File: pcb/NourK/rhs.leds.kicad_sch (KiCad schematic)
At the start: 33 parts

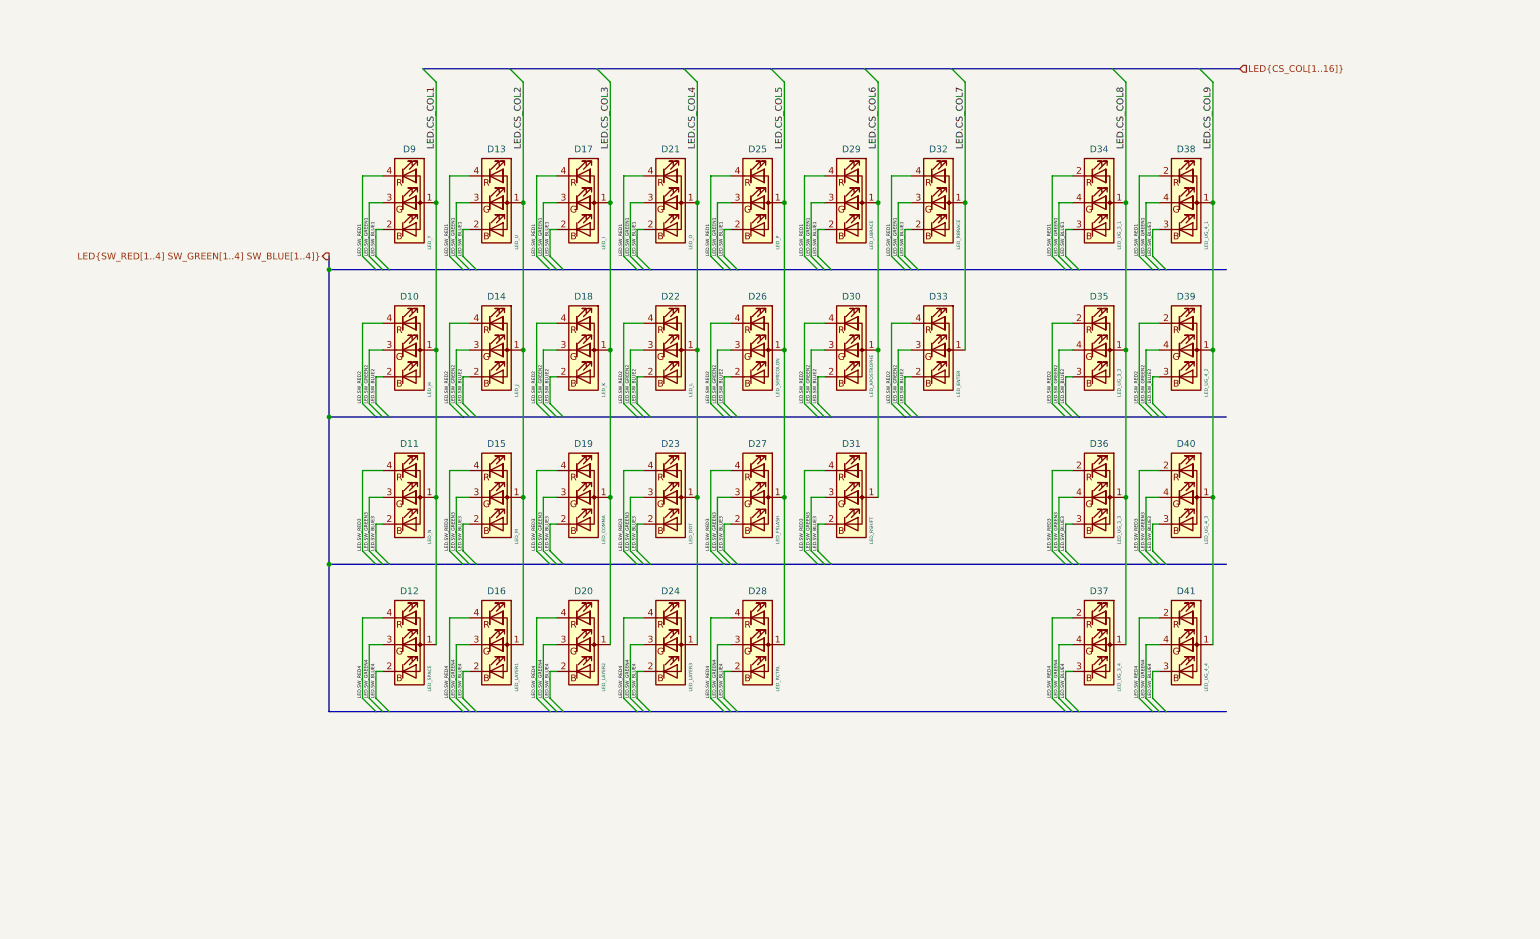
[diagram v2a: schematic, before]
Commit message: Re-traced RHS
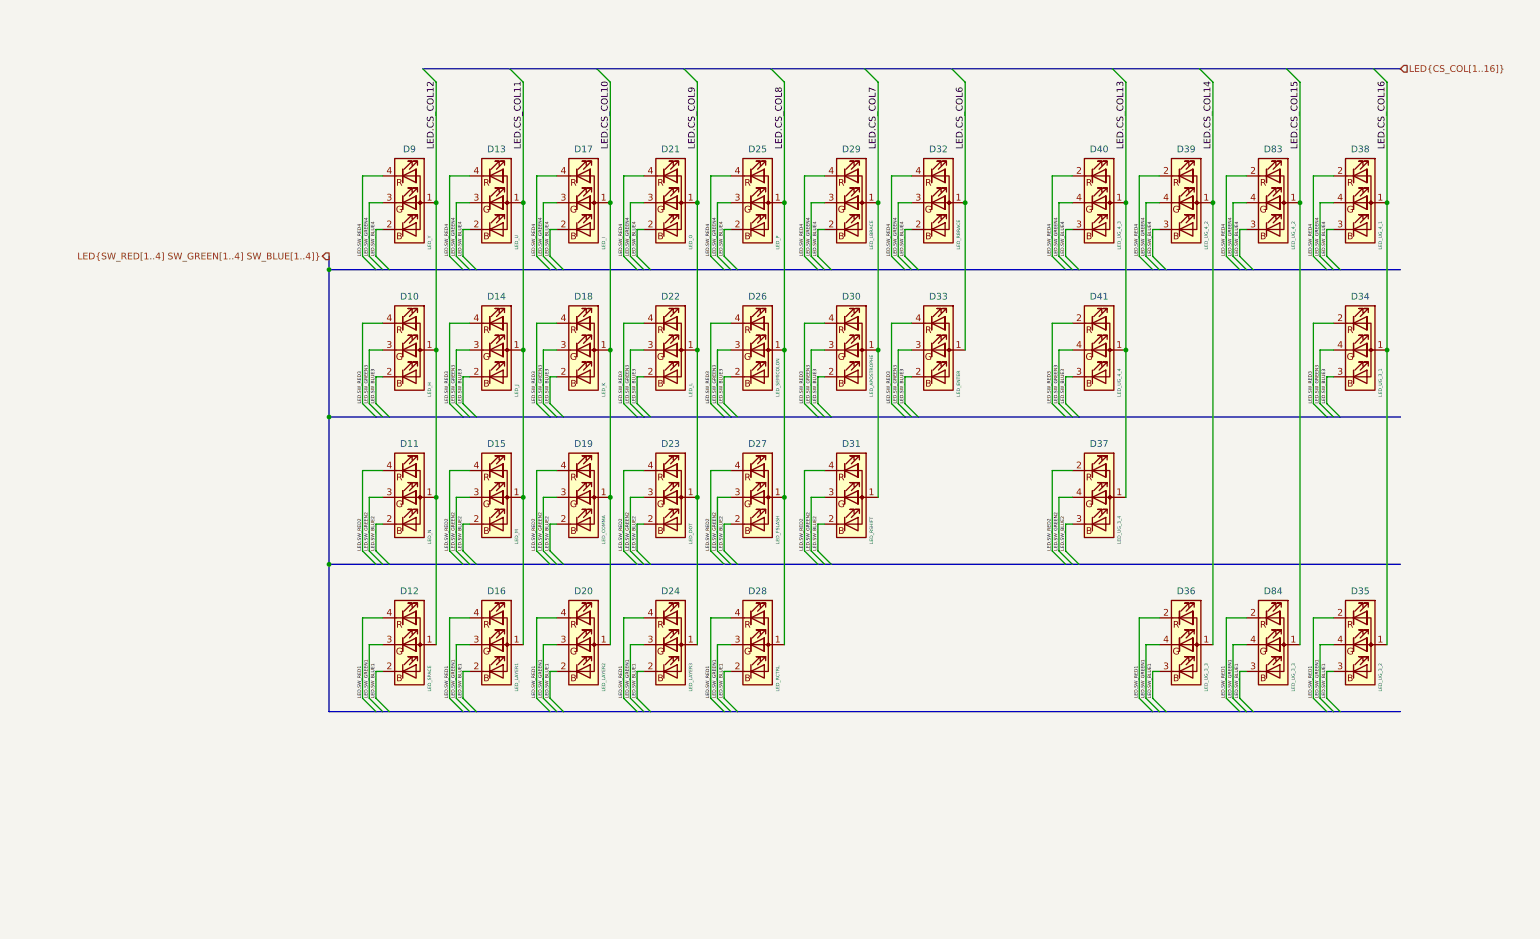
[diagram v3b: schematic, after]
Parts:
- added D83: LED_UG_4_2, Nour_KB:LTRBR37G4R4S012502R18, symbol Device:LED_ARBG
- added D84: LED_UG_3_3, Nour_KB:LTRBR37G4R4S012502R18, symbol Device:LED_ARBG
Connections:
- net LED.CS_COL4 is gone; now on net LED.CS_COL9: D21.1 (A), D22.1 (A), D23.1 (A), D24.1 (A)
- net LED.CS_COL5 is gone; now on net LED.CS_COL8: D25.1 (A), D26.1 (A), D27.1 (A), D28.1 (A)
- net LED.CS_COL6: now also D32.1 (A), D33.1 (A); no longer D29.1 (A), D30.1 (A), D31.1 (A)
- net LED.CS_COL7: now also D29.1 (A), D30.1 (A), D31.1 (A); no longer D32.1 (A), D33.1 (A)
- net LED.CS_COL8: no longer D34.1 (A), D35.1 (A), D36.1 (A), D37.1 (A)
- net LED.CS_COL9: no longer D38.1 (A), D39.1 (A), D40.1 (A), D41.1 (A)
- net LED.SW_BLUE1: now also D12.2 (BK), D16.2 (BK), D20.2 (BK), D24.2 (BK), D28.2 (BK), D35.3 (BK), D36.3 (BK), D84.3 (BK); no longer D13.2 (BK), D17.2 (BK), D21.2 (BK), D25.2 (BK), D29.2 (BK), D32.2 (BK), D34.3 (BK), D38.3 (BK), D9.2 (BK)
- net LED.SW_BLUE2: now also D11.2 (BK), D15.2 (BK), D19.2 (BK), D23.2 (BK), D27.2 (BK), D31.2 (BK), D37.3 (BK); no longer D10.2 (BK), D14.2 (BK), D18.2 (BK), D22.2 (BK), D26.2 (BK), D30.2 (BK), D33.2 (BK), D35.3 (BK), D39.3 (BK)
- net LED.SW_BLUE3: now also D10.2 (BK), D14.2 (BK), D18.2 (BK), D22.2 (BK), D26.2 (BK), D30.2 (BK), D33.2 (BK), D34.3 (BK), D41.3 (BK); no longer D11.2 (BK), D15.2 (BK), D19.2 (BK), D23.2 (BK), D27.2 (BK), D31.2 (BK), D36.3 (BK), D40.3 (BK)
- net LED.SW_BLUE4: now also D13.2 (BK), D17.2 (BK), D21.2 (BK), D25.2 (BK), D29.2 (BK), D32.2 (BK), D38.3 (BK), D39.3 (BK), D40.3 (BK), D9.2 (BK), D83.3 (BK); no longer D12.2 (BK), D16.2 (BK), D20.2 (BK), D24.2 (BK), D28.2 (BK), D37.3 (BK), D41.3 (BK)
- net LED.SW_GREEN1: now also D12.3 (GK), D16.3 (GK), D20.3 (GK), D24.3 (GK), D28.3 (GK), D35.4 (GK), D36.4 (GK), D84.4 (GK); no longer D13.3 (GK), D17.3 (GK), D21.3 (GK), D25.3 (GK), D29.3 (GK), D32.3 (GK), D34.4 (GK), D38.4 (GK), D9.3 (GK)
- net LED.SW_GREEN2: now also D11.3 (GK), D15.3 (GK), D19.3 (GK), D23.3 (GK), D27.3 (GK), D31.3 (GK), D37.4 (GK); no longer D10.3 (GK), D14.3 (GK), D18.3 (GK), D22.3 (GK), D26.3 (GK), D30.3 (GK), D33.3 (GK), D35.4 (GK), D39.4 (GK)
- net LED.SW_GREEN3: now also D10.3 (GK), D14.3 (GK), D18.3 (GK), D22.3 (GK), D26.3 (GK), D30.3 (GK), D33.3 (GK), D34.4 (GK), D41.4 (GK); no longer D11.3 (GK), D15.3 (GK), D19.3 (GK), D23.3 (GK), D27.3 (GK), D31.3 (GK), D36.4 (GK), D40.4 (GK)
- net LED.SW_GREEN4: now also D13.3 (GK), D17.3 (GK), D21.3 (GK), D25.3 (GK), D29.3 (GK), D32.3 (GK), D38.4 (GK), D39.4 (GK), D40.4 (GK), D9.3 (GK), D83.4 (GK); no longer D12.3 (GK), D16.3 (GK), D20.3 (GK), D24.3 (GK), D28.3 (GK), D37.4 (GK), D41.4 (GK)
- net LED.SW_RED1: now also D12.4 (RK), D16.4 (RK), D20.4 (RK), D24.4 (RK), D28.4 (RK), D35.2 (RK), D36.2 (RK), D84.2 (RK); no longer D13.4 (RK), D17.4 (RK), D21.4 (RK), D25.4 (RK), D29.4 (RK), D32.4 (RK), D34.2 (RK), D38.2 (RK), D9.4 (RK)
- net LED.SW_RED2: now also D11.4 (RK), D15.4 (RK), D19.4 (RK), D23.4 (RK), D27.4 (RK), D31.4 (RK), D37.2 (RK); no longer D10.4 (RK), D14.4 (RK), D18.4 (RK), D22.4 (RK), D26.4 (RK), D30.4 (RK), D33.4 (RK), D35.2 (RK), D39.2 (RK)
- net LED.SW_RED3: now also D10.4 (RK), D14.4 (RK), D18.4 (RK), D22.4 (RK), D26.4 (RK), D30.4 (RK), D33.4 (RK), D34.2 (RK), D41.2 (RK); no longer D11.4 (RK), D15.4 (RK), D19.4 (RK), D23.4 (RK), D27.4 (RK), D31.4 (RK), D36.2 (RK), D40.2 (RK)
- net LED.SW_RED4: now also D13.4 (RK), D17.4 (RK), D21.4 (RK), D25.4 (RK), D29.4 (RK), D32.4 (RK), D38.2 (RK), D39.2 (RK), D40.2 (RK), D9.4 (RK), D83.2 (RK); no longer D12.4 (RK), D16.4 (RK), D20.4 (RK), D24.4 (RK), D28.4 (RK), D37.2 (RK), D41.2 (RK)
- net LED.CS_COL1 renamed LED.CS_COL12
- net LED.CS_COL2 renamed LED.CS_COL11
- net LED.CS_COL3 renamed LED.CS_COL10
- new net LED.CS_COL13: D37.1 (A), D40.1 (A), D41.1 (A)
- new net LED.CS_COL14: D36.1 (A), D39.1 (A)
- new net LED.CS_COL15: D83.1 (A), D84.1 (A)
- new net LED.CS_COL16: D34.1 (A), D35.1 (A), D38.1 (A)
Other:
- moved on the sheet: D34, D35, D36, D37, D38, D39, D40, D41
